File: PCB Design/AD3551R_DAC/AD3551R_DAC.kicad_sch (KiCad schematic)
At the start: 0 parts

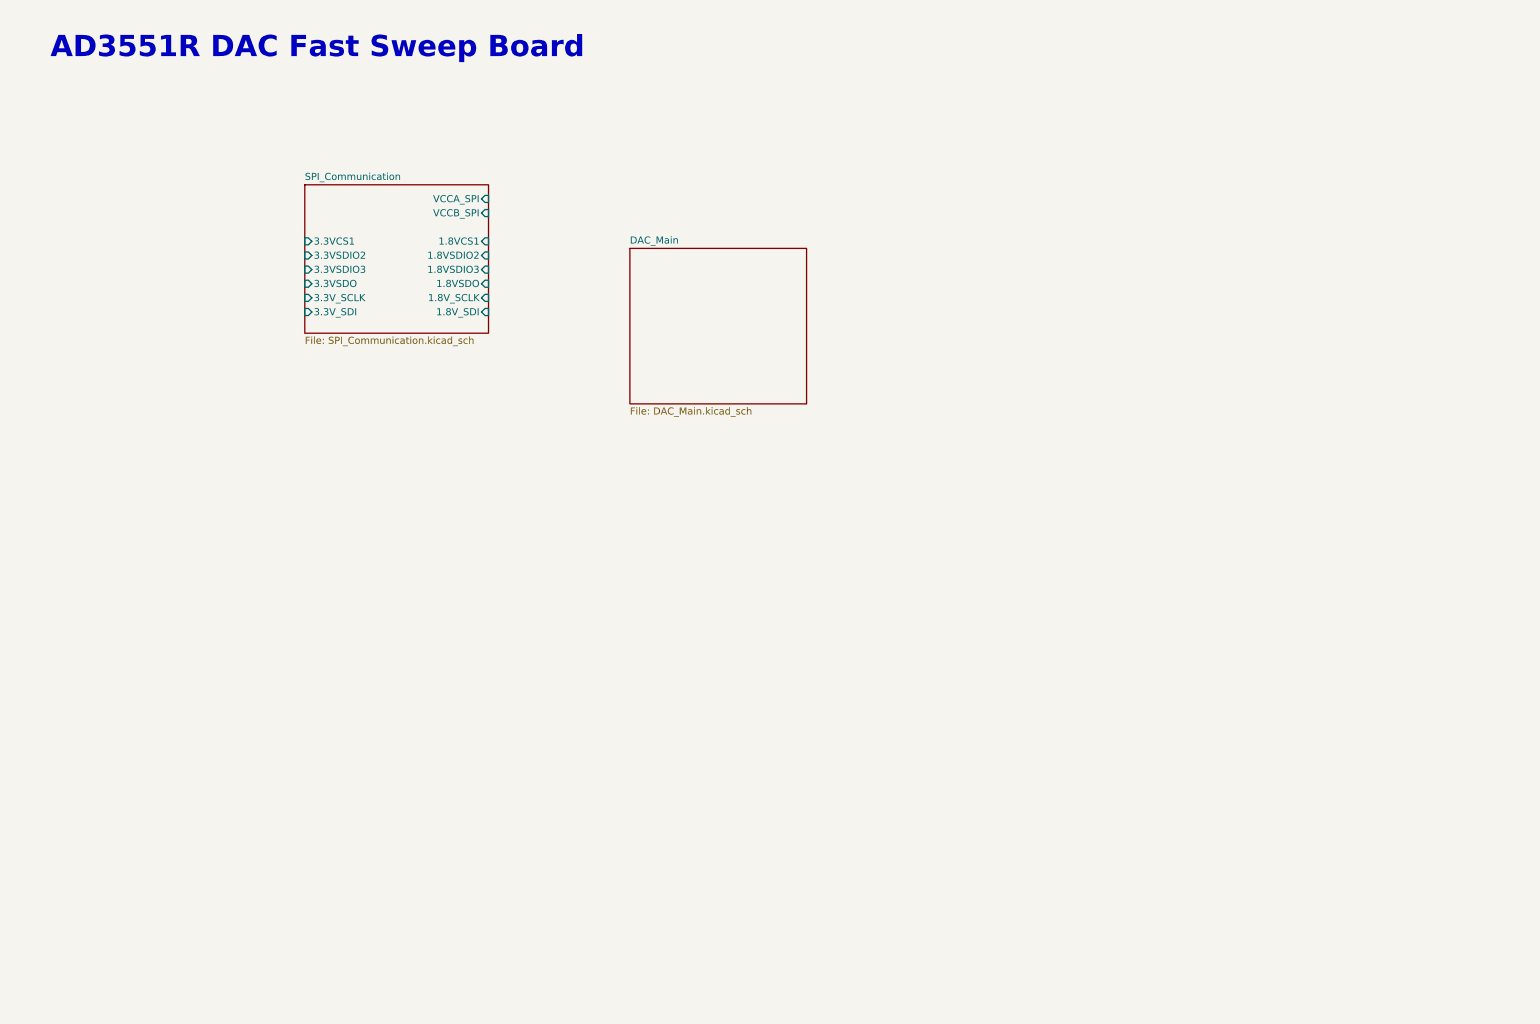
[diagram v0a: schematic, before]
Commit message: Schematic V1 Done and Up for Review
Schematic Done and into Review
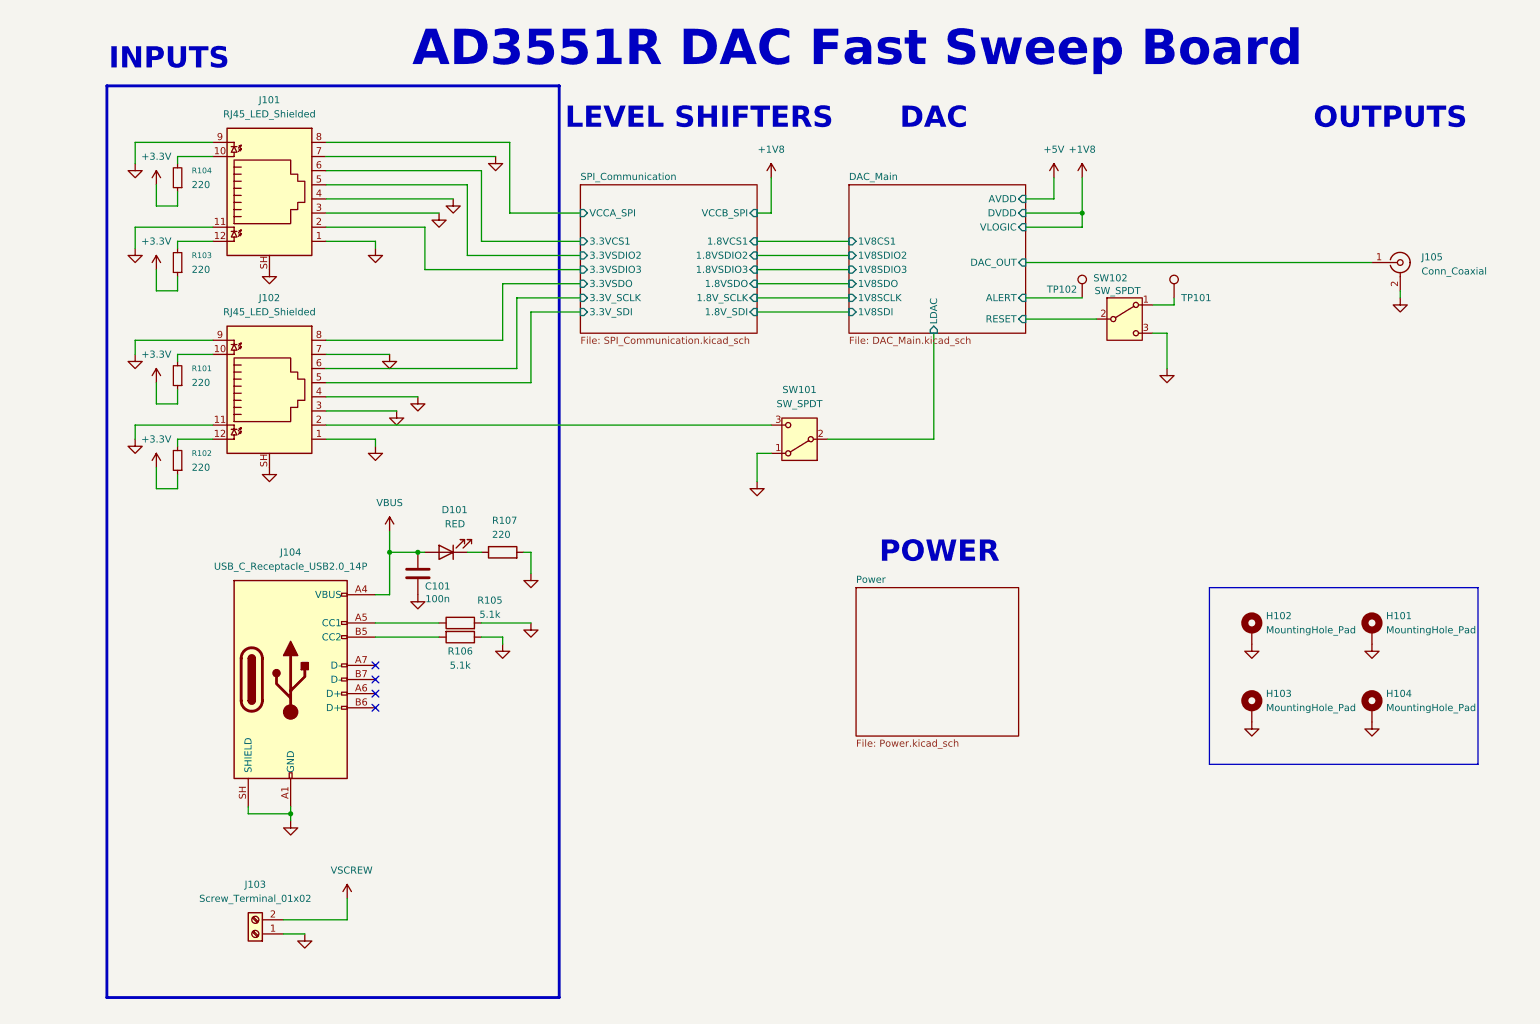
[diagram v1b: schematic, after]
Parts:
- added C101: 100n, Capacitor_SMD:C_0603_1608Metric, symbol Device:C
- added D101: RED, LED_SMD:LED_0603_1608Metric_Pad1.05x0.95mm_HandSolder, symbol Device:LED
- added H101, H102, H103, H104: MountingHole_Pad, symbol Mechanical:MountingHole_Pad
- added J101, J102: RJ45_LED_Shielded, symbol Connector:RJ45_LED_Shielded
- added J103: Screw_Terminal_01x02, symbol Connector:Screw_Terminal_01x02
- added J104: USB_C_Receptacle_USB2.0_14P, symbol Connector:USB_C_Receptacle_USB2.0_14P
- added J105: Conn_Coaxial, symbol Connector:Conn_Coaxial
- added R101, R102, R103, R104: 220, symbol Device:R_Small
- added R105, R106: 5.1k, symbol Device:R
- added R107: 220, Resistor_SMD:R_0603_1608Metric_Pad0.98x0.95mm_HandSolder, symbol Device:R
- added SW101, SW102: SW_SPDT, symbol Switch:SW_SPDT
- added TP101, TP102: TestPoint, symbol Connector:TestPoint
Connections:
- net SPI_Communication/3.3VCS1: now also J101.6
- net SPI_Communication/3.3VSDIO2: now also J101.5
- net SPI_Communication/3.3VSDIO3: now also J101.2
- net SPI_Communication/3.3VSDO: now also J102.8
- net SPI_Communication/3.3V_SCLK: now also J102.6
- net SPI_Communication/3.3V_SDI: now also J102.5
- net SPI_Communication/VCCA_SPI: now also J101.8
- new net: D101.1 (K), R107.1
- new net: SW102.1 (A), TP101.1
- new net: J101.10, R104.2
- new net: J101.12, R103.2
- new net: J104.A5 (CC1), R105.1
- new net: J104.B5 (CC2), R106.2
- new net: J102.10, R101.2
- new net: J102.2, SW101.3 (C)
- new net: J102.12, R102.2
- new net +3.3V: R101.1, R102.1, R103.1, R104.1
- new net DAC_Main/ALERT: TP102.1
- new net DAC_Main/DAC_OUT: J105.1 (In)
- new net DAC_Main/LDAC: SW101.2 (B)
- new net DAC_Main/RESET: SW102.2 (B)
- new net GND: C101.2, H101.1, H102.1, H103.1, H104.1, J101.1, J101.11, J101.3, J101.4, J101.7, J101.9, J101.SH, J102.1, J102.11, J102.3, J102.4, J102.7, J102.9, J102.SH, J103.1 (Pin_1), J104.A1 (GND), J104.A12 (GND), J104.B1 (GND), J104.B12 (GND), J104.SH (SHIELD), J105.2 (Ext), R105.2, R106.1, R107.2, SW101.1 (A), SW102.3 (C)
- new net VBUS: C101.1, D101.2 (A), J104.A4 (VBUS), J104.A9 (VBUS), J104.B4 (VBUS), J104.B9 (VBUS)
- new net VSCREW: J103.2 (Pin_2)
- no-connect marks 0 -> 4
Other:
- added sheet Power (Power.kicad_sch)
- sheet DAC_Main ports: added 1V8CS1, 1V8SCLK, 1V8SDI, 1V8SDIO2, 1V8SDIO3, 1V8SDO, ALERT, AVDD, DAC_OUT, DVDD, LDAC, RESET, VLOGIC; removed none
- note added: "DAC"
- note added: "INPUTS"
- note added: "LEVEL SHIFTERS"
- note added: "OUTPUTS"
- note added: "POWER"

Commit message: decoupling
decoupling
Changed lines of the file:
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@@
 		(dnp no)
 		(property "Reference" "R105"
-			(at 85.344 119.126 90)
+			(at 80.264 118.618 90)
 			(show_name no)
 			(do_not_autoplace no)
@@
 		)
 		(property "Value" "5.1k"
-			(at 85.344 121.666 90)
+			(at 80.264 121.158 90)
 			(show_name no)
 			(do_not_autoplace no)

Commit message: Changes
Changes
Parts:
- C101: value 100n -> 100nF
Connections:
- net GND: now also R105.1; no longer R105.2
- net at J104.A5 (CC1): now also R105.2; no longer R105.1
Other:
- note added: "+5V +3.3V +1.8V"
- note added: "3.3V"
- moved on the sheet: H101, H102, H103, H104, R105, R106

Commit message: PCB
PCB Layout started
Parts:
- H101, H102, H103, H104: footprint (none) -> MountingHole:MountingHole_5.3mm_M5_Pad
- J101, J102: footprint (none) -> Connector_RJ:RJ45_Abracon_ARJP11A-MA_Horizontal
- J103: footprint (none) -> TerminalBlock_Phoenix:TerminalBlock_Phoenix_PTSM-0,5-2-2.5-V-THR_1x02_P2.50mm_Vertical
- J104: footprint (none) -> Parts_fab:SAMESKY_UJ20-C-H-G-SMT-1-P16-TR
- J105: footprint (none) -> Connector_Coaxial:SMA_Amphenol_132289_EdgeMount
- R101, R102, R103, R104, R105, R106: footprint (none) -> Resistor_SMD:R_0603_1608Metric_Pad0.98x0.95mm_HandSolder
- SW101, SW102: footprint (none) -> Parts_fab:toggle_switch
- TP101, TP102: footprint (none) -> TestPoint:TestPoint_Plated_Hole_D2.0mm
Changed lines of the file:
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@@
 			)
 		)
-		(property "Footprint" ""
+		(property "Footprint" "TestPoint:TestPoint_Plated_Hole_D2.0mm"
 			(at 196.85 64.77 0)
 			(hide yes)
@@
 			)
 		)
-		(property "Footprint" ""
+		(property "Footprint" "MountingHole:MountingHole_5.3mm_M5_Pad"
 			(at 118.11 127 0)
 			(hide yes)
@@
 			)
 		)
-		(property "Footprint" ""
+		(property "Footprint" "Parts_fab:toggle_switch"
 			(at 199.39 68.58 0)
 			(hide yes)
@@
 			)
 		)
-		(property "Footprint" ""
+		(property "Footprint" "Connector_RJ:RJ45_Abracon_ARJP11A-MA_Horizontal"
 			(at 45.72 46.355 90)
 			(hide yes)
@@
 			)
 		)
-		(property "Footprint" ""
+		(property "Footprint" "Parts_fab:SAMESKY_UJ20-C-H-G-SMT-1-P16-TR"
 			(at 53.34 133.35 0)
 			(hide yes)
@@
 			)
 		)
-		(property "Footprint" ""
+		(property "Footprint" "TerminalBlock_Phoenix:TerminalBlock_Phoenix_PTSM-0,5-2-2.5-V-THR_1x02_P2.50mm_Vertical"
 			(at 43.18 179.07 0)
 			(hide yes)
@@
 			)
 		)
-		(property "Footprint" ""
+		(property "Footprint" "MountingHole:MountingHole_5.3mm_M5_Pad"
 			(at 118.11 113.03 0)
 			(hide yes)
@@
 			)
 		)
-		(property "Footprint" ""
+		(property "Footprint" "Resistor_SMD:R_0603_1608Metric_Pad0.98x0.95mm_HandSolder"
 			(at 29.21 78.74 0)
 			(hide yes)
@@
 			)
 		)
-		(property "Footprint" ""
+		(property "Footprint" "Parts_fab:toggle_switch"
 			(at 140.97 90.17 0)
 			(hide yes)
@@
 			)
 		)
-		(property "Footprint" ""
+		(property "Footprint" "Resistor_SMD:R_0603_1608Metric_Pad0.98x0.95mm_HandSolder"
 			(at 29.21 93.98 0)
 			(hide yes)
@@
 			)
 		)
-		(property "Footprint" ""
+		(property "Footprint" "TestPoint:TestPoint_Plated_Hole_D2.0mm"
 			(at 213.36 64.77 0)
 			(hide yes)
@@
 			)
 		)
-		(property "Footprint" ""
+		(property "Footprint" "Resistor_SMD:R_0603_1608Metric_Pad0.98x0.95mm_HandSolder"
 			(at 80.518 130.81 90)
 			(hide yes)
@@
 			)
 		)
-		(property "Footprint" ""
+		(property "Footprint" "MountingHole:MountingHole_5.3mm_M5_Pad"
 			(at 106.68 127 0)
 			(hide yes)
@@
 			)
 		)
-		(property "Footprint" ""
+		(property "Footprint" "MountingHole:MountingHole_5.3mm_M5_Pad"
 			(at 106.68 113.03 0)
 			(hide yes)
@@
 			)
 		)
-		(property "Footprint" ""
+		(property "Footprint" "Connector_Coaxial:SMA_Amphenol_132289_EdgeMount"
 			(at 248.92 58.42 0)
 			(hide yes)
@@
 			)
 		)
-		(property "Footprint" ""
+		(property "Footprint" "Connector_RJ:RJ45_Abracon_ARJP11A-MA_Horizontal"
 			(at 45.72 81.915 90)
 			(hide yes)
@@
 			)
 		)
-		(property "Footprint" ""
+		(property "Footprint" "Resistor_SMD:R_0603_1608Metric_Pad0.98x0.95mm_HandSolder"
 			(at 29.21 58.42 0)
 			(hide yes)
@@
 			)
 		)
-		(property "Footprint" ""
+		(property "Footprint" "Resistor_SMD:R_0603_1608Metric_Pad0.98x0.95mm_HandSolder"
 			(at 85.598 130.81 90)
 			(hide yes)
@@
 			)
 		)
-		(property "Footprint" ""
+		(property "Footprint" "Resistor_SMD:R_0603_1608Metric_Pad0.98x0.95mm_HandSolder"
 			(at 29.21 43.18 0)
 			(hide yes)
